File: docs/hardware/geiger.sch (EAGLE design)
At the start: 33 parts, among them U2 WIFI-32NO_TEXT, U4 BSP125

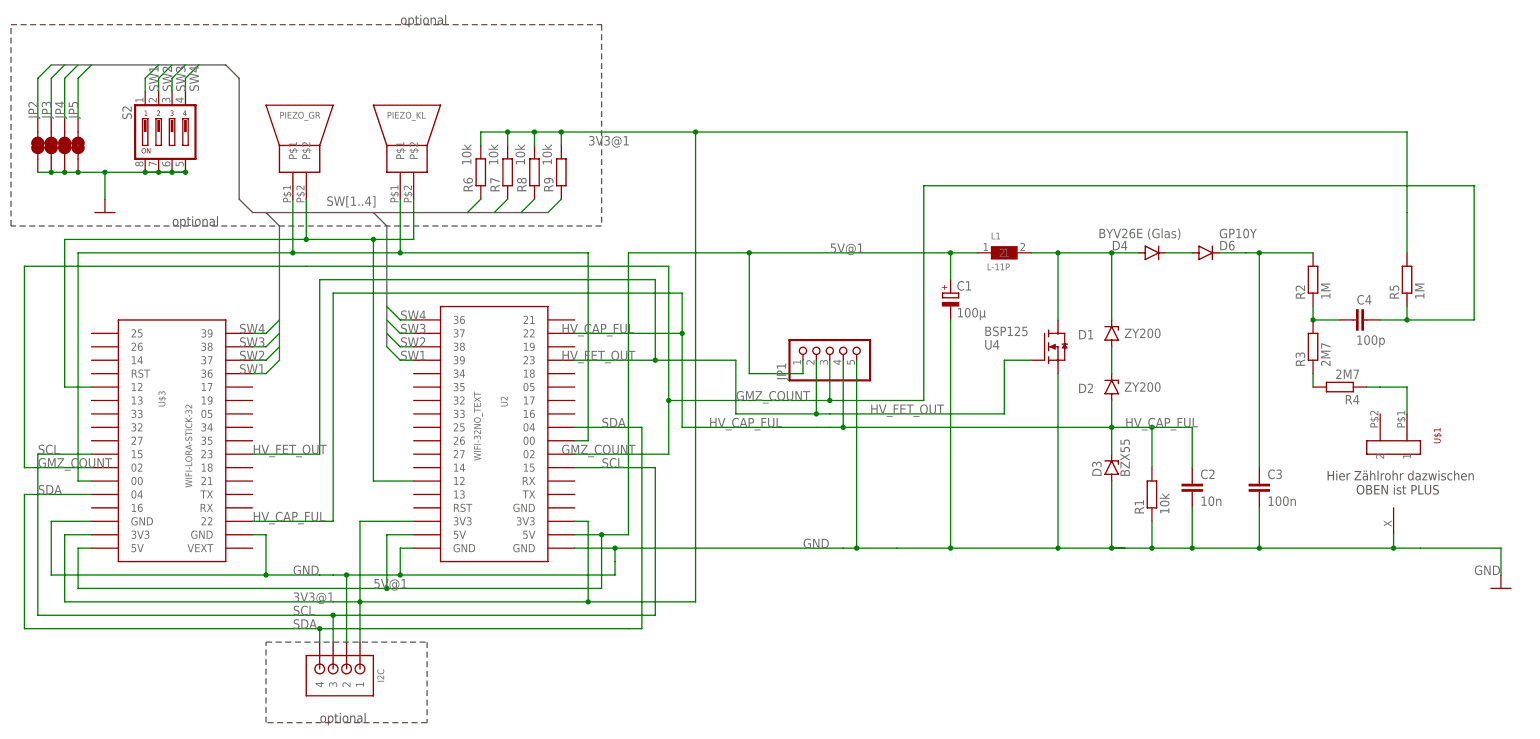
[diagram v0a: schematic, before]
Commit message: fixed schematic/layout error with new hardware
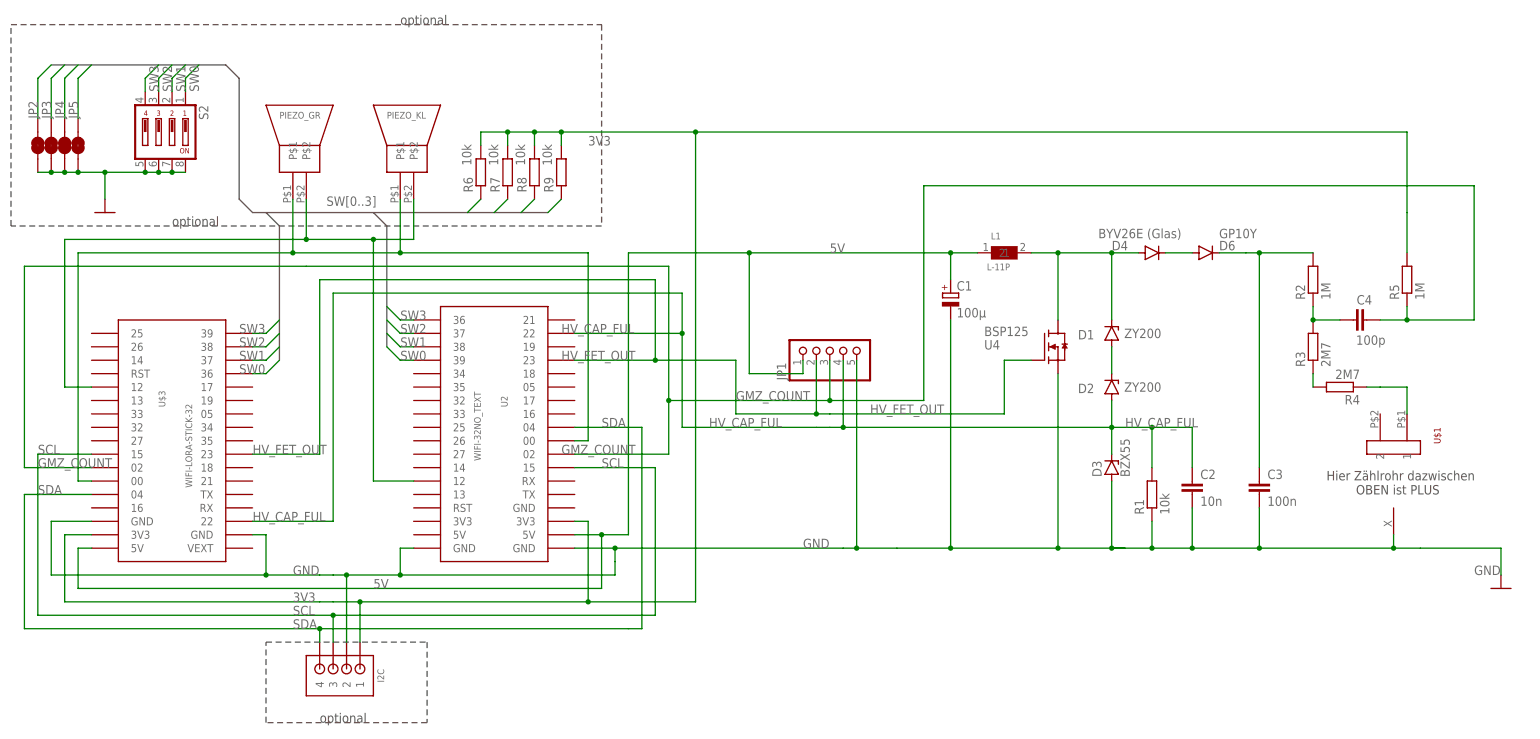
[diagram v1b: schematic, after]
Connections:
- removed net 3V3@1: I2C.1, R5.2, R6.2, R7.2, R8.2, R9.2, U$3.3V3, U2.3V3@1, U2.3V3@2
- removed net 5V@1: C1.+, JP1.1, L1.1, U$3.5V, U2.5V@1, U2.5V@2
- removed net SW4: JP2.2, R9.1, S2.4, U$3.39, U2.36
- new net 3V3: I2C.1, R5.2, R6.2, R7.2, R8.2, R9.2, U$3.3V3, U2.3V3@2
- new net 5V: C1.+, JP1.1, L1.1, U$3.5V, U2.5V@2
- new net SW0: JP5.2, R6.1, S2.1, U$3.36, U2.39
- net SW1: now also JP4.2, R7.1, S2.2, U$3.37, U2.38; no longer JP5.2, R6.1, S2.1, U$3.36, U2.39
- net SW2: now also JP3.2, R8.1, S2.3, U$3.38, U2.37; no longer JP4.2, R7.1, S2.2, U$3.37, U2.38
- net SW3: now also JP2.2, R9.1, S2.4, U$3.39, U2.36; no longer JP3.2, R8.1, S2.3, U$3.38, U2.37

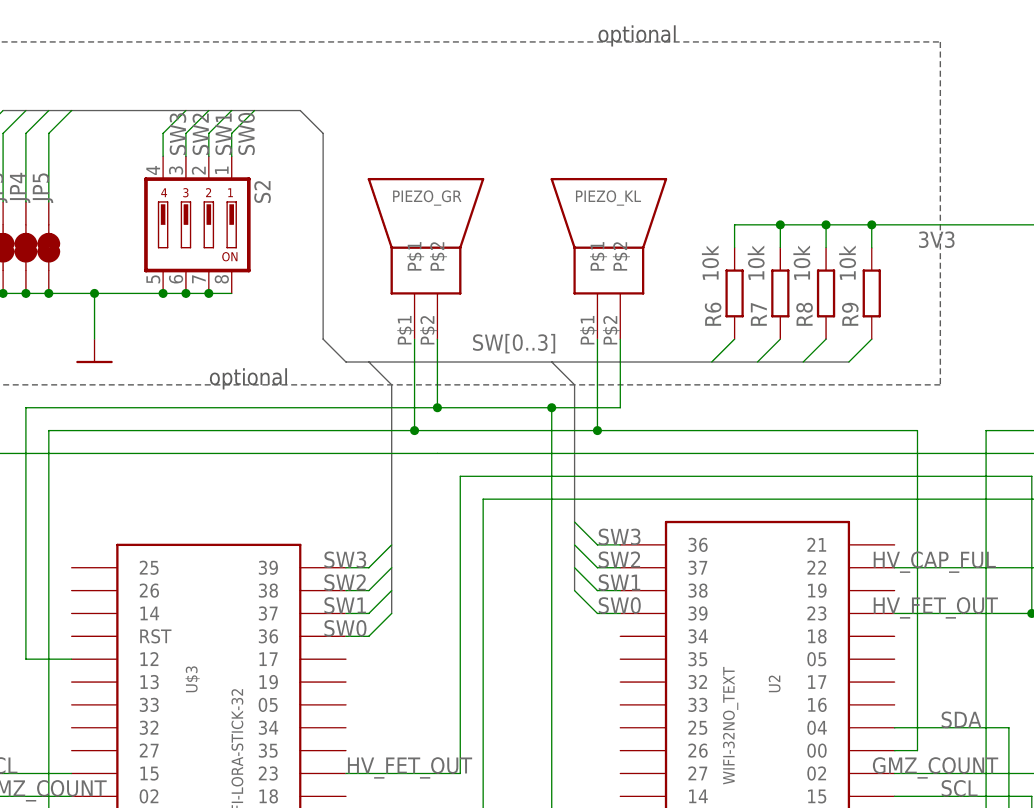
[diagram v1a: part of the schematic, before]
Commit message: Changed switch numbering,  fixes #349
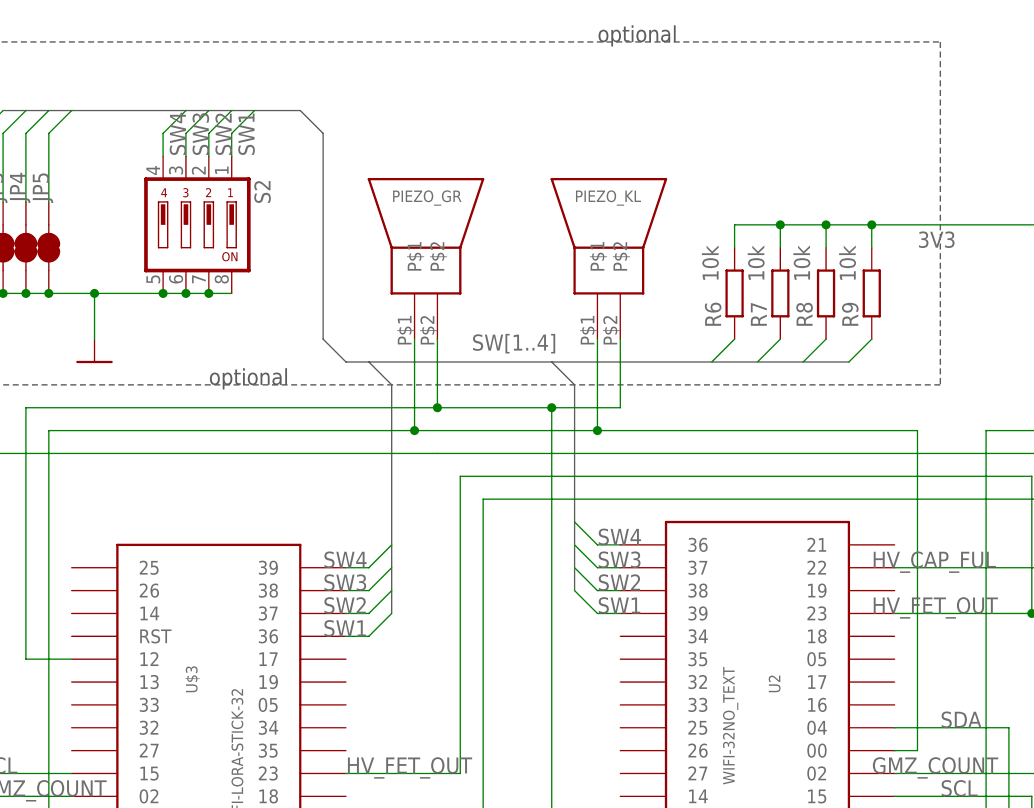
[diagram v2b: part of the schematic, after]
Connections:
- removed net SW0: JP5.2, R6.1, S2.1, U$3.36, U2.39
- new net SW4: JP2.2, R9.1, S2.4, U$3.39, U2.36
- net SW1: now also JP5.2, R6.1, S2.1, U$3.36, U2.39; no longer JP4.2, R7.1, S2.2, U$3.37, U2.38
- net SW2: now also JP4.2, R7.1, S2.2, U$3.37, U2.38; no longer JP3.2, R8.1, S2.3, U$3.38, U2.37
- net SW3: now also JP3.2, R8.1, S2.3, U$3.38, U2.37; no longer JP2.2, R9.1, S2.4, U$3.39, U2.36
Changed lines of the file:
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@@
 </instances>
 <busses>
-<bus name="SW[0..3]">
+<bus name="SW[1..4]">
 <segment>
 <wire x1="-71.12" y1="63.5" x2="-71.12" y2="88.9" width="0.762" layer="92"/>
@@
 <net name="SW3" class="0">
 <segment>
-<pinref part="U$3" gate="G$1" pin="39"/>
-<wire x1="-76.2" y1="68.58" x2="-73.66" y2="68.58" width="0.1524" layer="91"/>
-<wire x1="-71.12" y1="71.12" x2="-73.66" y2="68.58" width="0.1524" layer="91"/>
-<label x="-78.74" y="68.58" size="1.778" layer="95"/>
-</segment>
-<segment>
-<wire x1="-20.32" y1="91.44" x2="-17.78" y2="93.98" width="0.1524" layer="91"/>
-<pinref part="R9" gate="G$1" pin="1"/>
-</segment>
-<segment>
-<pinref part="U2" gate="G$1" pin="36"/>
-<wire x1="-50.8" y1="73.66" x2="-48.26" y2="71.12" width="0.1524" layer="91"/>
-<wire x1="-48.26" y1="71.12" x2="-45.72" y2="71.12" width="0.1524" layer="91"/>
-<label x="-48.26" y="71.12" size="1.778" layer="95"/>
-</segment>
-<segment>
-<wire x1="-93.98" y1="119.38" x2="-96.52" y2="116.84" width="0.1524" layer="91"/>
-<pinref part="S2" gate="1" pin="4"/>
-<wire x1="-96.52" y1="116.84" x2="-96.52" y2="114.3" width="0.1524" layer="91"/>
-<label x="-93.98" y="114.3" size="1.778" layer="95" rot="R90"/>
-</segment>
-<segment>
-<wire x1="-114.3" y1="119.38" x2="-116.84" y2="116.84" width="0.1524" layer="91"/>
-<pinref part="JP2" gate="G$1" pin="2"/>
-<wire x1="-116.84" y1="116.84" x2="-116.84" y2="109.22" width="0.1524" layer="91"/>
-</segment>
-</net>
-<net name="SW2" class="0">
-<segment>
-<wire x1="-71.12" y1="68.58" x2="-73.66" y2="66.04" width="0.1524" layer="91"/>
 <pinref part="U$3" gate="G$1" pin="38"/>
 <wire x1="-73.66" y1="66.04" x2="-76.2" y2="66.04" width="0.1524" layer="91"/>
 <label x="-78.74" y="66.04" size="1.778" layer="95"/>
-</segment>
-<segment>
-<wire x1="-25.4" y1="91.44" x2="-22.86" y2="93.98" width="0.1524" layer="91"/>
-<pinref part="R8" gate="G$1" pin="1"/>
+<wire x1="-73.66" y1="66.04" x2="-71.12" y2="68.58" width="0.1524" layer="91"/>
 </segment>
 <segment>
 <pinref part="U2" gate="G$1" pin="37"/>
-<wire x1="-50.8" y1="71.12" x2="-48.26" y2="68.58" width="0.1524" layer="91"/>
 <wire x1="-48.26" y1="68.58" x2="-45.72" y2="68.58" width="0.1524" layer="91"/>
 <label x="-48.26" y="68.58" size="1.778" layer="95"/>
+<wire x1="-48.26" y1="68.58" x2="-50.8" y2="71.12" width="0.1524" layer="91"/>
+</segment>
+<segment>
+<pinref part="R8" gate="G$1" pin="1"/>
+<wire x1="-22.86" y1="93.98" x2="-25.4" y2="91.44" width="0.1524" layer="91"/>
 </segment>
 <segment>
@@
 </segment>
 <segment>
-<wire x1="-111.76" y1="119.38" x2="-114.3" y2="116.84" width="0.1524" layer="91"/>
 <pinref part="JP3" gate="G$1" pin="2"/>
 <wire x1="-114.3" y1="116.84" x2="-114.3" y2="109.22" width="0.1524" layer="91"/>
-</segment>
-</net>
-<net name="SW1" class="0">
-<segment>
-<wire x1="-71.12" y1="66.04" x2="-73.66" y2="63.5" width="0.1524" layer="91"/>
+<wire x1="-111.76" y1="119.38" x2="-114.3" y2="116.84" width="0.1524" layer="91"/>
+</segment>
+</net>
+<net name="SW2" class="0">
+<segment>
 <pinref part="U$3" gate="G$1" pin="37"/>
 <wire x1="-73.66" y1="63.5" x2="-76.2" y2="63.5" width="0.1524" layer="91"/>
 <label x="-78.74" y="63.5" size="1.778" layer="95"/>
-</segment>
-<segment>
-<wire x1="-30.48" y1="91.44" x2="-27.94" y2="93.98" width="0.1524" layer="91"/>
-<pinref part="R7" gate="G$1" pin="1"/>
-</segment>
-<segment>
-<wire x1="-50.8" y1="68.58" x2="-48.26" y2="66.04" width="0.1524" layer="91"/>
+<wire x1="-73.66" y1="63.5" x2="-71.12" y2="66.04" width="0.1524" layer="91"/>
+</segment>
+<segment>
 <pinref part="U2" gate="G$1" pin="38"/>
 <wire x1="-48.26" y1="66.04" x2="-45.72" y2="66.04" width="0.1524" layer="91"/>
 <label x="-48.26" y="66.04" size="1.778" layer="95"/>
+<wire x1="-48.26" y1="66.04" x2="-50.8" y2="68.58" width="0.1524" layer="91"/>
+</segment>
+<segment>
+<pinref part="R7" gate="G$1" pin="1"/>
+<wire x1="-27.94" y1="93.98" x2="-30.48" y2="91.44" width="0.1524" layer="91"/>
 </segment>
 <segment>
@@
 </segment>
 <segment>
-<wire x1="-109.22" y1="119.38" x2="-111.76" y2="116.84" width="0.1524" layer="91"/>
 <pinref part="JP4" gate="G$1" pin="2"/>
 <wire x1="-111.76" y1="116.84" x2="-111.76" y2="109.22" width="0.1524" layer="91"/>
-</segment>
-</net>
-<net name="SW0" class="0">
-<segment>
-<wire x1="-71.12" y1="63.5" x2="-73.66" y2="60.96" width="0.1524" layer="91"/>
+<wire x1="-109.22" y1="119.38" x2="-111.76" y2="116.84" width="0.1524" layer="91"/>
+</segment>
+</net>
+<net name="SW1" class="0">
+<segment>
 <pinref part="U$3" gate="G$1" pin="36"/>
 <wire x1="-73.66" y1="60.96" x2="-76.2" y2="60.96" width="0.1524" layer="91"/>
 <label x="-78.74" y="60.96" size="1.778" layer="95"/>
-</segment>
-<segment>
-<wire x1="-35.56" y1="91.44" x2="-33.02" y2="93.98" width="0.1524" layer="91"/>
-<pinref part="R6" gate="G$1" pin="1"/>
-</segment>
-<segment>
-<wire x1="-50.8" y1="66.04" x2="-48.26" y2="63.5" width="0.1524" layer="91"/>
+<wire x1="-73.66" y1="60.96" x2="-71.12" y2="63.5" width="0.1524" layer="91"/>
+</segment>
+<segment>
 <pinref part="U2" gate="G$1" pin="39"/>
 <wire x1="-48.26" y1="63.5" x2="-45.72" y2="63.5" width="0.1524" layer="91"/>
 <label x="-48.26" y="63.5" size="1.778" layer="95"/>
+<wire x1="-48.26" y1="63.5" x2="-50.8" y2="66.04" width="0.1524" layer="91"/>
+</segment>
+<segment>
+<pinref part="R6" gate="G$1" pin="1"/>
+<wire x1="-33.02" y1="93.98" x2="-35.56" y2="91.44" width="0.1524" layer="91"/>
 </segment>
 <segment>
@@
 </segment>
 <segment>
-<wire x1="-106.68" y1="119.38" x2="-109.22" y2="116.84" width="0.1524" layer="91"/>
 <pinref part="JP5" gate="G$1" pin="2"/>
 <wire x1="-109.22" y1="116.84" x2="-109.22" y2="109.22" width="0.1524" layer="91"/>
+<wire x1="-106.68" y1="119.38" x2="-109.22" y2="116.84" width="0.1524" layer="91"/>
 </segment>
 </net>
@@
 </segment>
 </net>
+<net name="SW4" class="0">
+<segment>
+<pinref part="U$3" gate="G$1" pin="39"/>
+<wire x1="-76.2" y1="68.58" x2="-73.66" y2="68.58" width="0.1524" layer="91"/>
+<label x="-78.74" y="68.58" size="1.778" layer="95"/>
+<wire x1="-73.66" y1="68.58" x2="-71.12" y2="71.12" width="0.1524" layer="91"/>
+</segment>
+<segment>
+<pinref part="U2" gate="G$1" pin="36"/>
+<wire x1="-48.26" y1="71.12" x2="-45.72" y2="71.12" width="0.1524" layer="91"/>
+<label x="-48.26" y="71.12" size="1.778" layer="95"/>
+<wire x1="-48.26" y1="71.12" x2="-50.8" y2="73.66" width="0.1524" layer="91"/>
+</segment>
+<segment>
+<pinref part="R9" gate="G$1" pin="1"/>
+<wire x1="-17.78" y1="93.98" x2="-20.32" y2="91.44" width="0.1524" layer="91"/>
+</segment>
+<segment>
+<wire x1="-93.98" y1="119.38" x2="-96.52" y2="116.84" width="0.1524" layer="91"/>
+<pinref part="S2" gate="1" pin="4"/>
+<wire x1="-96.52" y1="116.84" x2="-96.52" y2="114.3" width="0.1524" layer="91"/>
+<label x="-93.98" y="114.3" size="1.778" layer="95" rot="R90"/>
+</segment>
+<segment>
+<pinref part="JP2" gate="G$1" pin="2"/>
+<wire x1="-116.84" y1="116.84" x2="-116.84" y2="109.22" width="0.1524" layer="91"/>
+<wire x1="-114.3" y1="119.38" x2="-116.84" y2="116.84" width="0.1524" layer="91"/>
+</segment>
+</net>

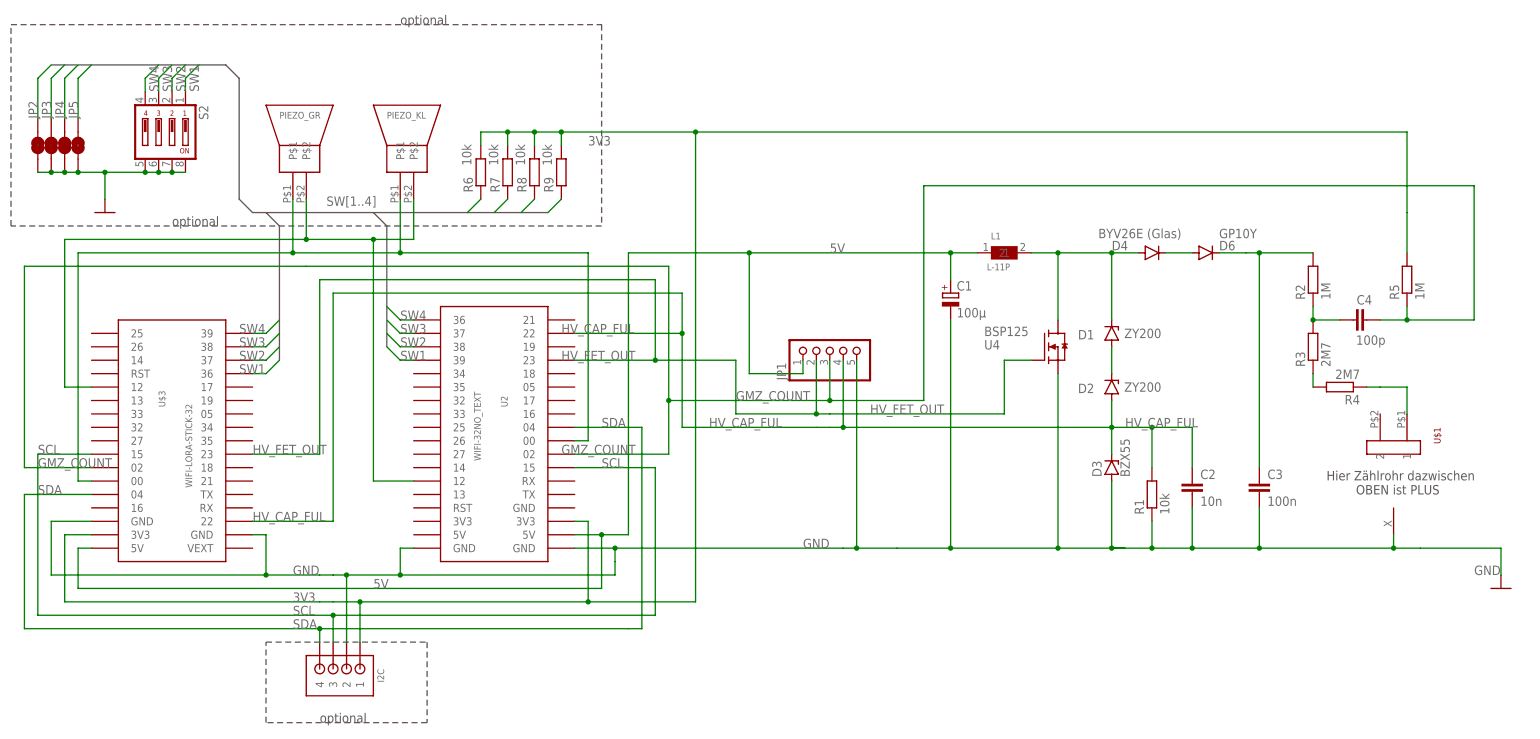
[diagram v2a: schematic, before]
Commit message: Switch numbering left to right
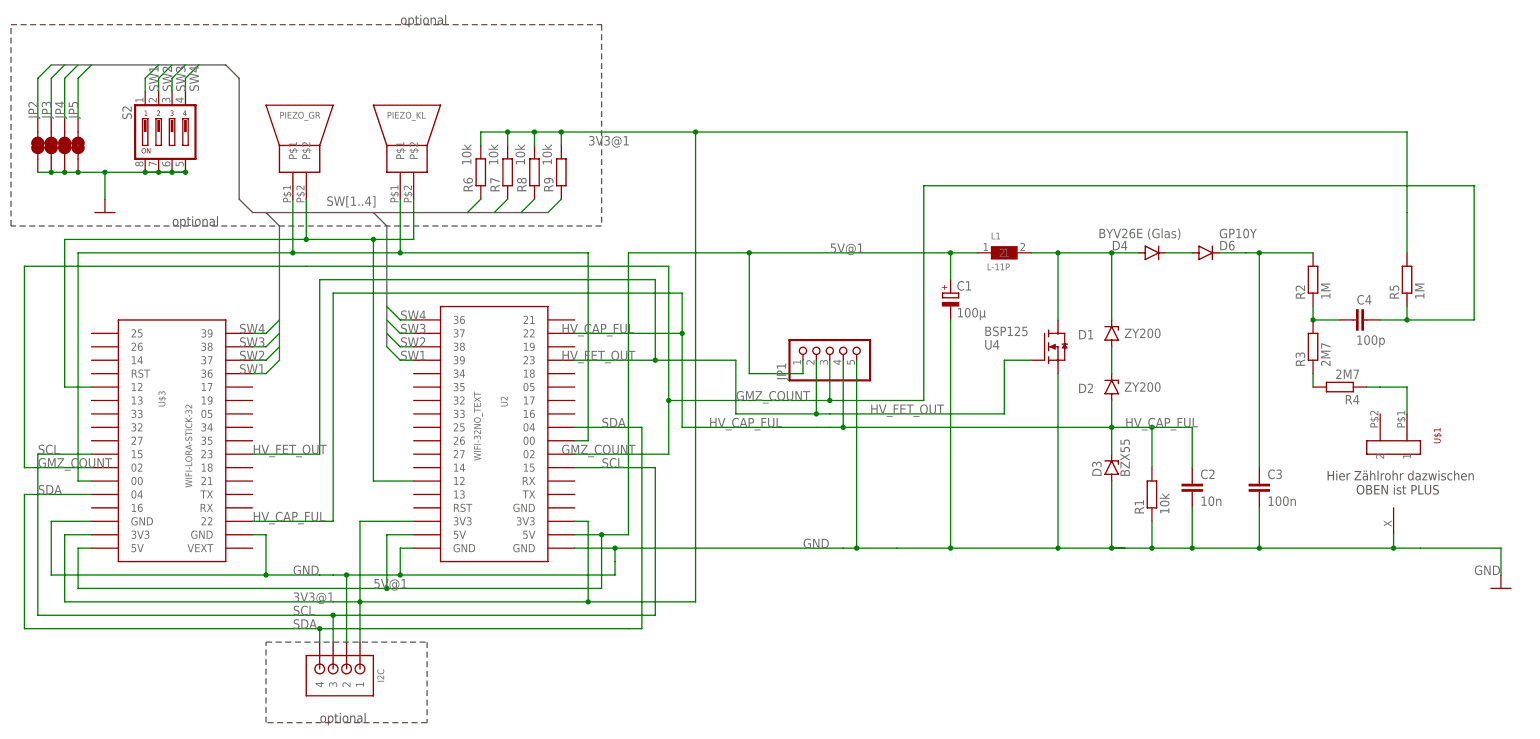
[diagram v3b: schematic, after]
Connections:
- removed net 3V3: I2C.1, R5.2, R6.2, R7.2, R8.2, R9.2, U$3.3V3, U2.3V3@2
- removed net 5V: C1.+, JP1.1, L1.1, U$3.5V, U2.5V@2
- new net 3V3@1: I2C.1, R5.2, R6.2, R7.2, R8.2, R9.2, U$3.3V3, U2.3V3@1, U2.3V3@2
- new net 5V@1: C1.+, JP1.1, L1.1, U$3.5V, U2.5V@1, U2.5V@2
